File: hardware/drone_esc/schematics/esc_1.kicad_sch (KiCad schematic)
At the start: 0 parts

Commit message: finished power section and one esc. need to finish the component assinment for jlcpcb and the rest of the esc
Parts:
- added C10, C8, C9: 0.47uF 25V X7R MLCC, Capacitor_SMD:C_0603_1608Metric, symbol Device:C
- added C11: 4.7uF 25V X7R MLCC, Capacitor_SMD:C_1206_3216Metric, symbol Device:C
- added C12, C14, C16: 47uF 35V X7R MLCC, Capacitor_SMD:C_2220_5750Metric, symbol Device:C
- added C13, C15, C17: 10nF 10V X7R MLCC, Capacitor_SMD:C_0402_1005Metric, symbol Device:C
- added D1, D2, D3: BAT165, Drone_components:BAT165, symbol Drone_components:BAT165
- added Q1, Q2, Q3, Q4, Q5, Q6: BSC016N04LS, Drone_components:BSC016N04LS, symbol Drone_components:BSC016N04LS
- added R10, R11, R2, R3, R6, R7: 33, Resistor_SMD:R_0402_1005Metric, symbol Device:R
- added R12, R4, R8: 4.7k, Resistor_SMD:R_0402_1005Metric, symbol Device:R
- added R13, R5, R9: 1k, Resistor_SMD:R_0402_1005Metric, symbol Device:R
- added U4: FD6288Q, Drone_components:FD6288Q, symbol Drone_components:FD6288Q
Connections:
- new net: C10.1, D3.1, U4.14 (VB3)
- new net: Q5.4, R10.2
- new net: Q2.4, R3.2
- new net: Q1.4, R2.2
- new net: C9.1, D2.1, U4.17 (VB2)
- new net: Q4.4, R7.2
- new net: Q3.4, R6.2
- new net: C8.1, D1.1, U4.20 (VB1)
- new net: Q6.4, R11.2
- new net GND: C11.1, C12.2, C13.2, C14.2, C15.2, C16.2, C17.2, Q2.1-3, Q4.1-3, Q6.1-3, R13.1, R5.1, R9.1, U4.25 (EXP), U4.6 (COM)
- new net HIN1A: U4.22 (HIN1)
- new net HIN1B: U4.23 (HIN2)
- new net HIN1C: U4.24 (HIN3)
- new net HO1: R2.1, U4.19 (HO1)
- new net HO2: R6.1, U4.16 (HO2)
- new net HO3: R10.1, U4.13 (HO3)
- new net LIN1A: U4.1 (LIN1)
- new net LIN1B: U4.2 (LIN2)
- new net LIN1C: U4.3 (LIN3)
- new net LO1: R3.1, U4.11 (LO1)
- new net LO2: R7.1, U4.10 (LO2)
- new net LO3: R11.1, U4.9 (LO3)
- new net VCC: C11.2, C12.1, C14.1, C16.1, D1.2, D2.2, D3.2, Q1.5-8, Q3.5-8, Q5.5-8, U4.4 (VCC)
- new net VS1: C8.2, Q1.1-3, Q2.5-8, R4.2, U4.18 (VS1)
- new net VS2: C9.2, Q3.1-3, Q4.5-8, R8.2, U4.15 (VS2)
- new net VS3: C10.2, Q5.1-3, Q6.5-8, R12.2, U4.12 (VS3)
- new net VSense1A: C13.1, R4.1, R5.2
- new net VSense1B: C15.1, R8.1, R9.2
- new net VSense1C: C17.1, R12.1, R13.2

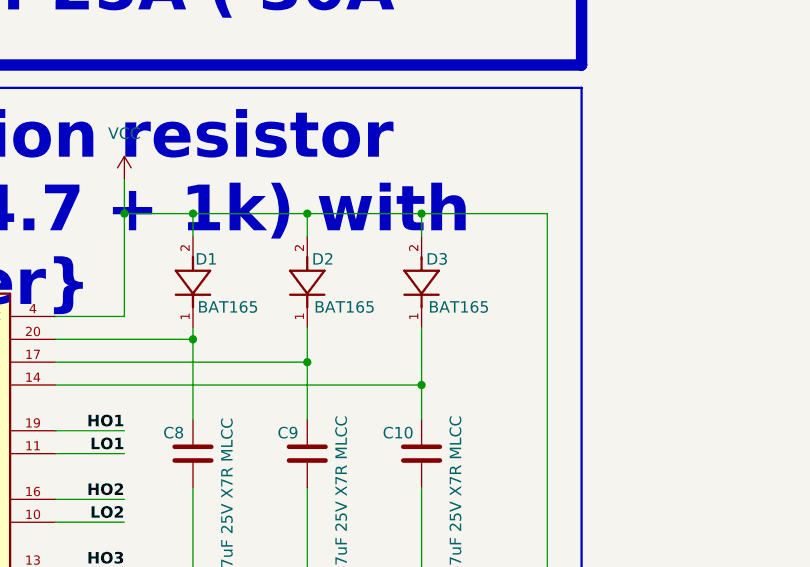
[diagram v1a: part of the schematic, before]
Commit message: finished 4 esc schematics need further refinment of the sheets
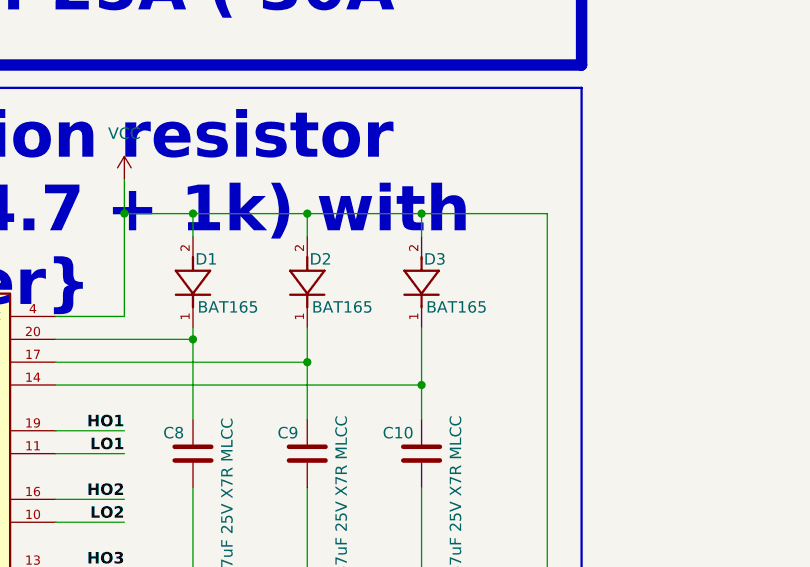
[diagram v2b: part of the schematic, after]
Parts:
- D1, D2, D3: JLCPCB part (none) -> C151511
- Q1, Q2, Q3, Q4, Q5, Q6: JLCPCB part (none) -> C534294
- U4: JLCPCB part (none) -> C328453

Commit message: continued developing the pcb board
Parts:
- C12, C14, C16: value 47uF 35V X7R MLCC -> 22uF 25V X5R MLCC; footprint Capacitor_SMD:C_2220_5750Metric -> Capacitor_SMD:C_1210_3225Metric; JLCPCB part C3873016 -> C12891
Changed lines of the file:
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@@
 	(symbol
 		(lib_id "Device:C")
-		(at 105.41 88.9 0)
-		(unit 1)
-		(exclude_from_sim no)
-		(in_bom yes)
-		(on_board yes)
-		(dnp no)
-		(fields_autoplaced yes)
-		(property "Reference" "C14"
-			(at 109.22 87.6299 0)
-			(effects
-				(font
-					(size 1.27 1.27)
-				)
-				(justify left)
-			)
-		)
-		(property "Value" "47uF 35V X7R MLCC"
-			(at 109.22 90.1699 0)
-			(effects
-				(font
-					(size 1.27 1.27)
-				)
-				(justify left)
-			)
-		)
-		(property "Footprint" "Capacitor_SMD:C_2220_5750Metric"
-			(at 106.3752 92.71 0)
-			(effects
-				(font
-					(size 1.27 1.27)
-				)
-				(hide yes)
-			)
-		)
-		(property "Datasheet" "~"
-			(at 105.41 88.9 0)
-			(effects
-				(font
-					(size 1.27 1.27)
-				)
-				(hide yes)
-			)
-		)
-		(property "Description" "Unpolarized capacitor"
-			(at 105.41 88.9 0)
-			(effects
-				(font
-					(size 1.27 1.27)
-				)
-				(hide yes)
-			)
-		)
-		(property "JLCPCB part" "C3873016"
-			(at 105.41 88.9 0)
-			(effects
-				(font
-					(size 1.27 1.27)
-				)
-				(hide yes)
-			)
-		)
-		(pin "2"
-		)
-		(pin "1"
-		)
-		(instances
-			(project "drone_esc"
-				(path "/b5a13fd4-6868-4fff-a56c-eae40f1d53c7/1c0adf10-7558-4c66-8a8d-f42e3254a4bc"
-					(reference "C14")
-					(unit 1)
-				)
-			)
-		)
-	)
-	(symbol
-		(lib_id "Device:C")
 		(at 264.16 115.57 0)
 		(unit 1)
@@
 	(symbol
 		(lib_id "Device:C")
-		(at 105.41 143.51 0)
+		(at 105.41 88.9 0)
 		(unit 1)
 		(exclude_from_sim no)
@@
 		(dnp no)
 		(fields_autoplaced yes)
-		(property "Reference" "C16"
-			(at 109.22 142.2399 0)
+		(property "Reference" "C14"
+			(at 109.22 87.6299 0)
 			(effects
 				(font
@@
 			)
 		)
-		(property "Value" "47uF 35V X7R MLCC"
-			(at 109.22 144.7799 0)
+		(property "Value" "22uF 25V X5R MLCC"
+			(at 109.22 90.1699 0)
 			(effects
 				(font
@@
 			)
 		)
-		(property "Footprint" "Capacitor_SMD:C_2220_5750Metric"
-			(at 106.3752 147.32 0)
+		(property "Footprint" "Capacitor_SMD:C_1210_3225Metric"
+			(at 106.3752 92.71 0)
 			(effects
 				(font
@@
 		)
 		(property "Datasheet" "~"
-			(at 105.41 143.51 0)
+			(at 105.41 88.9 0)
 			(effects
 				(font
@@
 		)
 		(property "Description" "Unpolarized capacitor"
-			(at 105.41 143.51 0)
+			(at 105.41 88.9 0)
 			(effects
 				(font
@@
 			)
 		)
-		(property "JLCPCB part" "C3873016"
-			(at 105.41 143.51 0)
+		(property "JLCPCB part" "C12891"
+			(at 105.41 88.9 0)
 			(effects
 				(font
@@
 			(project "drone_esc"
 				(path "/b5a13fd4-6868-4fff-a56c-eae40f1d53c7/1c0adf10-7558-4c66-8a8d-f42e3254a4bc"
-					(reference "C16")
+					(reference "C14")
 					(unit 1)
 				)
@@
 	)
 	(symbol
+		(lib_id "Device:C")
+		(at 105.41 143.51 0)
+		(unit 1)
+		(exclude_from_sim no)
+		(in_bom yes)
+		(on_board yes)
+		(dnp no)
+		(fields_autoplaced yes)
+		(property "Reference" "C16"
+			(at 109.22 142.2399 0)
+			(effects
+				(font
+					(size 1.27 1.27)
+				)
+				(justify left)
+			)
+		)
+		(property "Value" "22uF 25V X5R MLCC"
+			(at 109.22 144.7799 0)
+			(effects
+				(font
+					(size 1.27 1.27)
+				)
+				(justify left)
+			)
+		)
+		(property "Footprint" "Capacitor_SMD:C_1210_3225Metric"
+			(at 106.3752 147.32 0)
+			(effects
+				(font
+					(size 1.27 1.27)
+				)
+				(hide yes)
+			)
+		)
+		(property "Datasheet" "~"
+			(at 105.41 143.51 0)
+			(effects
+				(font
+					(size 1.27 1.27)
+				)
+				(hide yes)
+			)
+		)
+		(property "Description" "Unpolarized capacitor"
+			(at 105.41 143.51 0)
+			(effects
+				(font
+					(size 1.27 1.27)
+				)
+				(hide yes)
+			)
+		)
+		(property "JLCPCB part" "C12891"
+			(at 105.41 143.51 0)
+			(effects
+				(font
+					(size 1.27 1.27)
+				)
+				(hide yes)
+			)
+		)
+		(pin "2"
+		)
+		(pin "1"
+		)
+		(instances
+			(project "drone_esc"
+				(path "/b5a13fd4-6868-4fff-a56c-eae40f1d53c7/1c0adf10-7558-4c66-8a8d-f42e3254a4bc"
+					(reference "C16")
+					(unit 1)
+				)
+			)
+		)
+	)
+	(symbol
 		(lib_id "power:GND")
 		(at 73.66 182.88 0)
@@
 			)
 		)
-		(property "Value" "47uF 35V X7R MLCC"
+		(property "Value" "22uF 25V X5R MLCC"
 			(at 109.22 36.8299 0)
 			(effects
@@
 			)
 		)
-		(property "Footprint" "Capacitor_SMD:C_2220_5750Metric"
+		(property "Footprint" "Capacitor_SMD:C_1210_3225Metric"
 			(at 106.3752 39.37 0)
 			(effects
@@
 			)
 		)
-		(property "JLCPCB part" "C3873016"
+		(property "JLCPCB part" "C12891"
 			(at 105.41 35.56 0)
 			(effects

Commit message: finnished component placement
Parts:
- removed D1, D2, D3: BAT165, Drone_components:BAT165, symbol Drone_components:BAT165
- added D1, D2, D3: RB520S30, Drone_components:RB520S30, symbol Drone_components:RB520S30
- C10, C8, C9: value 0.47uF 25V X7R MLCC -> 1uF 25V X5R MLCC; footprint Capacitor_SMD:C_0603_1608Metric -> Capacitor_SMD:C_0402_1005Metric; JLCPCB part C1623 -> C52923
- C11: value 4.7uF 25V X7R MLCC -> 10uF 25V X5R MLCC; footprint Capacitor_SMD:C_1206_3216Metric -> Capacitor_SMD:C_0603_1608Metric; JLCPCB part C29823 -> C96446
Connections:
- net VCC: now also D1.2, D2.2, D3.2
- net at C10.1, U4.14 (VB3): now also D3.1
- net at C9.1, U4.17 (VB2): now also D2.1
- net at C8.1, U4.20 (VB1): now also D1.1

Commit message: replaced some of the schematics
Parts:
- removed Q1, Q2, Q3, Q4, Q5, Q6: BSC016N04LS, Drone_components:BSC016N04LS, symbol Drone_components:BSC016N04LS
- added Q1, Q2, Q3, Q4, Q5, Q6: BSC009NE2LS5IATMA1, Drone_components:BSC093N04LSGATMA1, symbol Drone_components:BSC009NE2LS5IATMA1
- C12, C14, C16: footprint Capacitor_SMD:C_1210_3225Metric -> Capacitor_SMD:C_0805_2012Metric; JLCPCB part C12891 -> C45783
- R10, R11, R2, R3, R6, R7: value 33 -> 10
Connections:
- net GND: now also Q2.1, Q2.2, Q2.3, Q4.1, Q4.2, Q4.3, Q6.1, Q6.2, Q6.3
- net VCC: now also Q1.5, Q3.5, Q5.5
- net VS1: now also Q1.1, Q1.2, Q1.3, Q2.5
- net VS2: now also Q3.1, Q3.2, Q3.3, Q4.5
- net VS3: now also Q5.1, Q5.2, Q5.3, Q6.5
- net at R11.2: now also Q6.4
- net at R2.2: now also Q1.4
- net at R10.2: now also Q5.4
- net at R3.2: now also Q2.4
- net at R6.2: now also Q3.4
- net at R7.2: now also Q4.4
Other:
- moved on the sheet: R10, R11, R2, R3, R6, R7

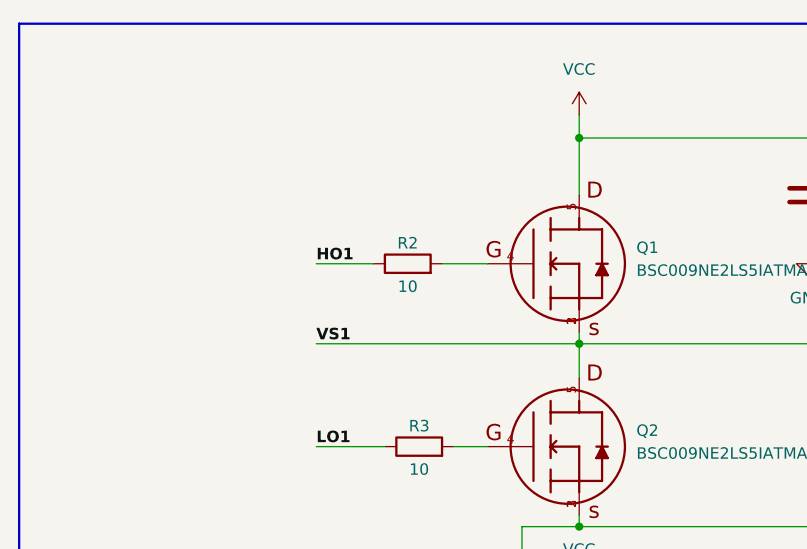
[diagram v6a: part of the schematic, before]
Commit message: changed some footprints and reconstracted the latout with better gate resistors clearence
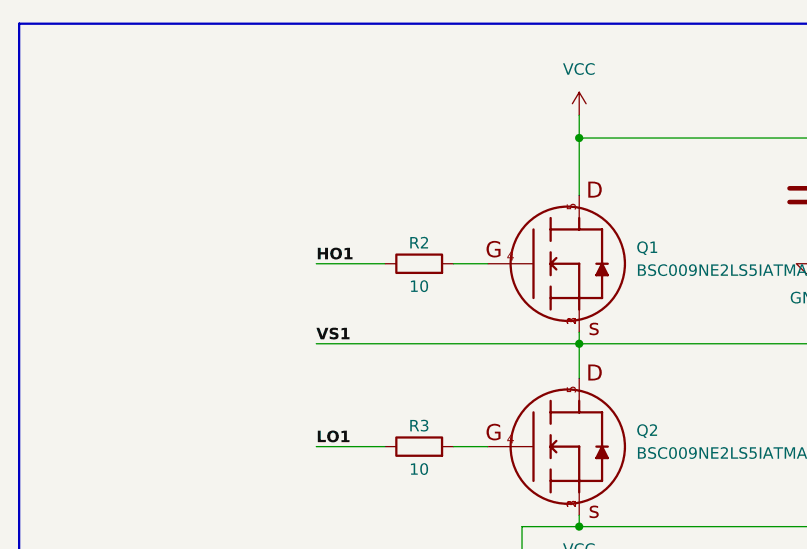
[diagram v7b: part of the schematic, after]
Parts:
- R10, R11, R2, R3, R6, R7: footprint Resistor_SMD:R_0402_1005Metric -> Resistor_SMD:R_0201_0603Metric; JLCPCB part C25105 -> C105889
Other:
- moved on the sheet: R2
